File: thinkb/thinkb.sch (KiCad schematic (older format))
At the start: 128 parts, among them SW1 SW_Push, SW2 SW_Push, SW3 SW_Push, SW4 SW_Push, SW5 SW_Push, SW6 SW_Push

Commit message: Working on the PCB
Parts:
- removed D? (x6): 1N4148, Diode_THT:D_DO-35_SOD27_P7.62mm_Horizontal, symbol Diode:1N4148
- removed SW? (x6): SW_Push, footprints:Choc_PG1350_Choc_Spacing, symbol Switch:SW_Push
- added D50, D59: 1N4148, footprints:diode_TH_SMD, symbol Diode:1N4148
- added SW50, SW59: SW_Push, footprints:Choc_PG1350_Choc_Spacing, symbol Switch:SW_Push
- D1, D2, D3, D4, D5, D6: footprint Diode_THT:D_DO-35_SOD27_P7.62mm_Horizontal -> footprints:diode_TH_SMD
- D10, D11, D12, D13, D14, D15, D16, D17, D18, D19, D20, D21, D22, D23, D24, D25, D26, D27, D28, D29, D30, D31, D32, D33, D34, D35, D36, D37, D38, D39, D40, D41, D42, D43, D44, D45, D46, D47, D48, D49, D51, D52, D53, D54, D55, D56, D57, D58, D60, D7, D8, D9: renamed from D?; footprint Diode_THT:D_DO-35_SOD27_P7.62mm_Horizontal -> footprints:diode_TH_SMD
- gave numbers to parts that had none: 52
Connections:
- net col12 is gone; now on net col10: SW11.2, SW23.2, SW35.2, SW47.2
- net col13 is gone; now on net col11: SW12.2, SW24.2, SW36.2, SW48.2, SW60.2
- net col1: now also SW50.2
- net col10: now also SW59.2; no longer SW21.2, SW33.2, SW45.2, SW57.2, SW9.2
- net col11: no longer SW10.2, SW22.2, SW34.2, SW46.2, SW58.2
- net col6: now also SW19.2, SW31.2, SW43.2, SW55.2, SW7.2
- net col7: now also SW20.2, SW32.2, SW44.2, SW56.2, SW8.2
- net col8: now also SW21.2, SW33.2, SW45.2, SW57.2, SW9.2; no longer SW19.2, SW31.2, SW43.2, SW55.2, SW7.2
- net col9: now also SW10.2, SW22.2, SW34.2, SW46.2, SW58.2; no longer SW20.2, SW32.2, SW44.2, SW56.2, SW8.2
- net row4: now also D50.1 (K), D59.1 (K)
- new net: D50.2 (A), SW50.1
- new net: D59.2 (A), SW59.1
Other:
- moved on the sheet: D10, D11, D12, D19, D20, D21, D22, D23, D24, D31, D32, D33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

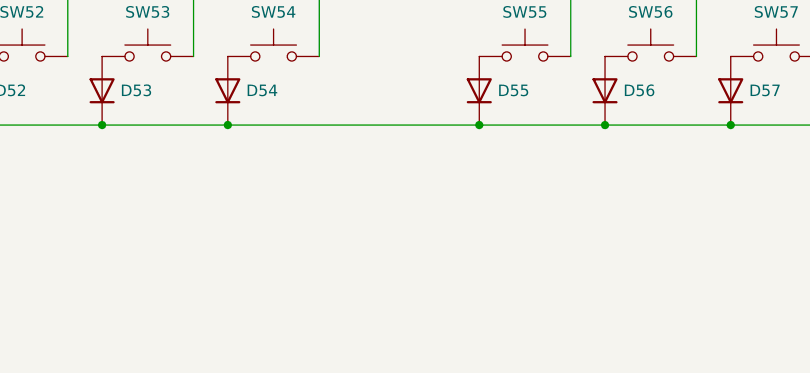
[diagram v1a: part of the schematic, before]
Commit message: Added rotary encoder
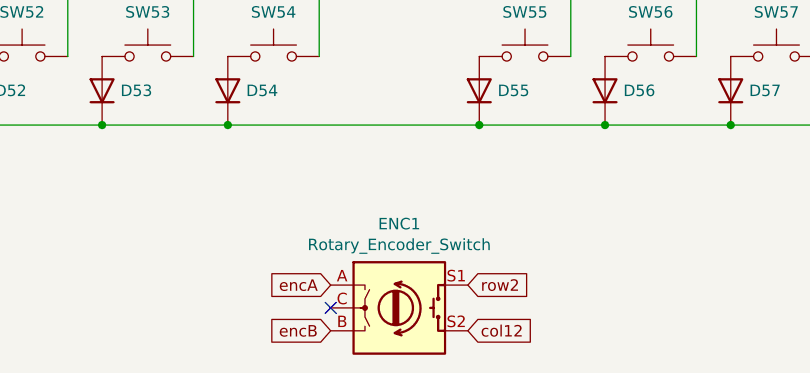
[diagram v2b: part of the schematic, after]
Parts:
- added ENC1: Rotary_Encoder_Switch, footprints:RotaryEncoder_Alps_EC11E, symbol Device:Rotary_Encoder_Switch
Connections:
- net row2: now also ENC1.S1
- new net col12: ENC1.S2
- new net encA: ENC1.A
- new net encB: ENC1.B
- no-connect marks 0 -> 1
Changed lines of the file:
@@
 	0    -1   -1   0
 $EndComp
+$Comp
+L Device:Rotary_Encoder_Switch ENC1
+U 1 1 616135F5
+P 4850 4700
+F 0 "ENC1" H 4850 5067 50  0000 C CNN
+F 1 "Rotary_Encoder_Switch" H 4850 4976 50  0000 C CNN
+F 2 "footprints:RotaryEncoder_Alps_EC11E" H 4700 4860 50  0001 C CNN
+F 3 "~" H 4850 4960 50  0001 C CNN
+	1    4850 4700
+	1    0    0    -1
+$EndComp
+Text GLabel 5150 4600 2    50   Input ~ 0
+row2
+Text GLabel 5150 4800 2    50   Input ~ 0
+col12
+Text GLabel 4550 4600 0    50   Input ~ 0
+encA
+NoConn ~ 4550 4700
+Text GLabel 4550 4800 0    50   Input ~ 0
+encB
 $EndSCHEMATC

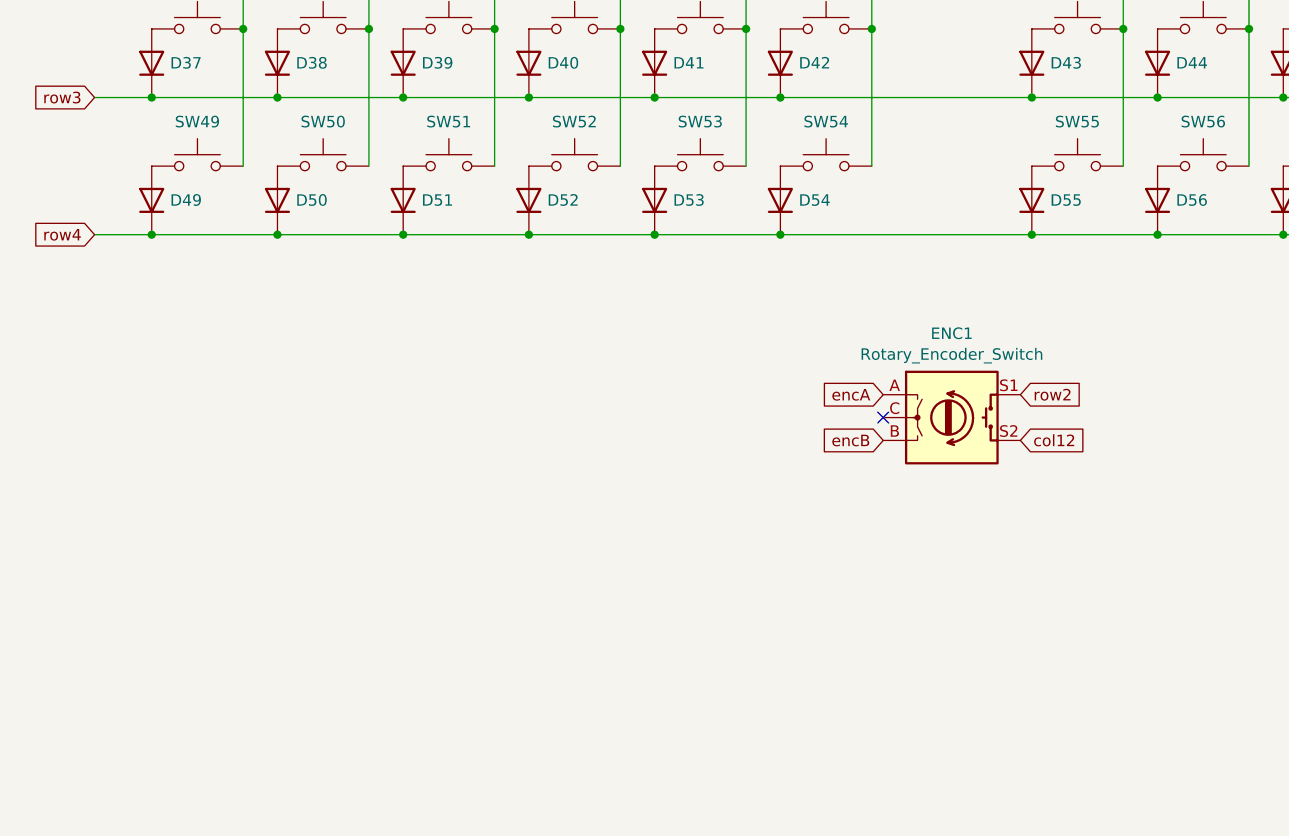
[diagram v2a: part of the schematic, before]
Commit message: Added promicro
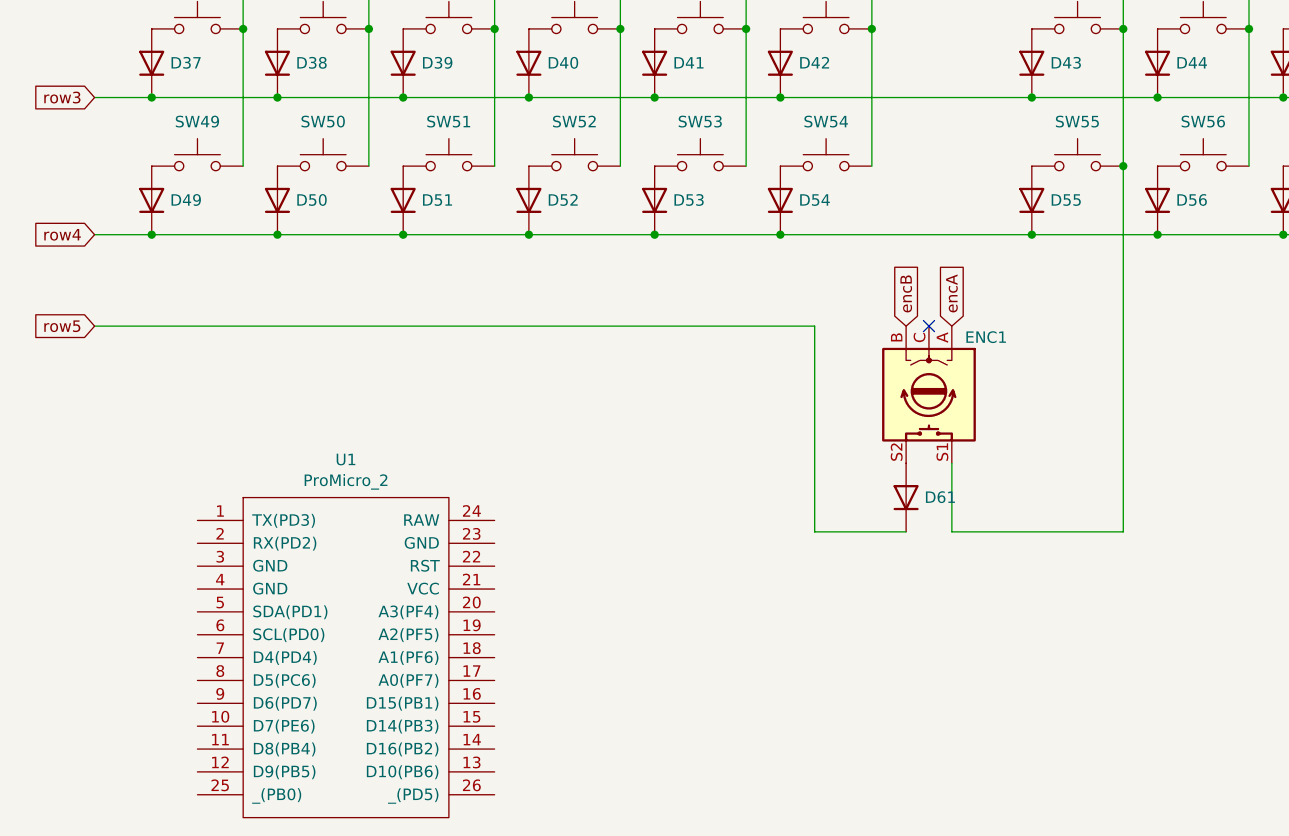
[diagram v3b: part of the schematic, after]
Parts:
- added D61: 1N4148, footprints:diode_TH_SMD, symbol Diode:1N4148
- added U1: ProMicro_2, footprints:ProMicro, symbol promicro_2:ProMicro_2
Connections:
- net col6: now also ENC1.S1
- net row2: no longer ENC1.S1
- net col12: no longer names the net of ENC1.S2
- net col12: now also D61.2 (A)
- new net row5: D61.1 (K)
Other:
- moved on the sheet: ENC1
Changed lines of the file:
@@
 	4100 2100 5200 2100
-Wire Wire Line
-	4100 2700 5200 2700
 Wire Wire Line
 	4100 3300 5200 3300
@@
 	0    -1   -1   0
 $EndComp
+Text GLabel 4850 4300 1    50   Input ~ 0
+encA
+NoConn ~ 4750 4300
+Text GLabel 4650 4300 1    50   Input ~ 0
+encB
+$Comp
+L Diode:1N4148 D61
+U 1 1 616F71C2
+P 4650 5050
+F 0 "D61" V 4650 4970 50  0000 R CNN
+F 1 "1N4148" H 4650 5176 50  0001 C CNN
+F 2 "footprints:diode_TH_SMD" H 4650 4875 50  0001 C CNN
+F 3 "https://assets.nexperia.com/documents/data-sheet/1N4148_1N4448.pdf" H 4650 5050 50  0001 C CNN
+	1    4650 5050
+	0    -1   -1   0
+$EndComp
 $Comp
 L Device:Rotary_Encoder_Switch ENC1
 U 1 1 616135F5
-P 4850 4700
-F 0 "ENC1" H 4850 5067 50  0000 C CNN
-F 1 "Rotary_Encoder_Switch" H 4850 4976 50  0000 C CNN
-F 2 "footprints:RotaryEncoder_Alps_EC11E" H 4700 4860 50  0001 C CNN
-F 3 "~" H 4850 4960 50  0001 C CNN
-	1    4850 4700
+P 4750 4600
+F 0 "ENC1" V 4500 4850 50  0000 C CNN
+F 1 "Rotary_Encoder_Switch" V 4500 5200 50  0001 C CNN
+F 2 "footprints:RotaryEncoder_Alps_EC11E" H 4600 4760 50  0001 C CNN
+F 3 "~" H 4750 4860 50  0001 C CNN
+	1    4750 4600
+	0    1    1    0
+$EndComp
+Wire Wire Line
+	4650 5200 4250 5200
+Wire Wire Line
+	4850 5200 4850 4900
+Wire Wire Line
+	4100 2700 5200 2700
+Text GLabel 1100 4300 0    50   Input ~ 0
+row5
+Wire Wire Line
+	1100 4300 4250 4300
+Wire Wire Line
+	4250 4300 4250 5200
+Wire Wire Line
+	5600 3600 5600 5200
+Wire Wire Line
+	5600 5200 4850 5200
+Connection ~ 5600 3600
+$Comp
+L promicro_2:ProMicro_2 U1
+U 1 1 6198CAAD
+P 2200 5700
+F 0 "U1" H 2200 6515 50  0000 C CNN
+F 1 "ProMicro_2" H 2200 6424 50  0000 C CNN
+F 2 "footprints:ProMicro" H 2150 5800 50  0001 C CNN
+F 3 "" H 2150 5800 50  0001 C CNN
+	1    2200 5700
 	1    0    0    -1
 $EndComp
-Text GLabel 5150 4600 2    50   Input ~ 0
-row2
-Text GLabel 5150 4800 2    50   Input ~ 0
-col12
-Text GLabel 4550 4600 0    50   Input ~ 0
-encA
-NoConn ~ 4550 4700
-Text GLabel 4550 4800 0    50   Input ~ 0
-encB
 $EndSCHEMATC

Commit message: Trying to implement more sophisticated row/col scheme
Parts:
- removed D10, D11, D12, D21, D22, D23, D24, D33, D34, D35, D36, D45, D46, D47, D48, D57, D58, D59, D60, D61, D9: 1N4148, footprints:diode_TH_SMD, symbol Diode:1N4148
- removed SW10, SW11, SW12, SW21, SW22, SW23, SW24, SW33, SW34, SW35, SW36, SW45, SW46, SW47, SW48, SW57, SW58, SW59, SW60, SW9: SW_Push, footprints:Choc_PG1350_Choc_Spacing, symbol Switch:SW_Push
- added D? (x23): 1N4148, footprints:diode_TH_SMD, symbol Diode:1N4148
- added SW? (x23): SW_Push, footprints:Choc_PG1350_Choc_Spacing, symbol Switch:SW_Push
- renumbered D13 to D9, SW13 to SW9
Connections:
- net col0: now also SW?.2, SW?.2, SW?.2
- net col1: now also SW?.2, SW?.2, SW?.2
- net col2: now also SW?.2, SW?.2, SW?.2
- net col3: now also ENC1.S2, SW?.2, SW?.2, SW?.2
- net col4: now also SW?.2, SW?.2
- net col5: now also SW?.2, SW?.2, SW?.2
- net col6: now also SW?.2, SW?.2, SW?.2; no longer ENC1.S1
- net col7: now also SW?.2, SW?.2, SW?.2
- net row5: now also D?.1 (K), D?.1 (K), D?.1 (K), D?.1 (K), D?.1 (K), D?.1 (K), D?.1 (K), D?.1 (K)
- new net: D?.2 (A), ENC1.S1, SW?.1
- new net: D?.2 (A), SW?.1 (x22)
- new net row6: D?.1 (K), D?.1 (K), D?.1 (K), D?.1 (K), D?.1 (K), D?.1 (K), D?.1 (K), D?.1 (K)
- new net row7: D?.1 (K), D?.1 (K), D?.1 (K), D?.1 (K), D?.1 (K), D?.1 (K), D?.1 (K)
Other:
- moved on the sheet: D17, D18, D29, D30, D41, D42, D5, D53, D54, D6, ENC1, SW17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

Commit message: WIP on keyboard matrix
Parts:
- removed D17, D4, D5: 1N4148, footprints:diode_TH_SMD, symbol Diode:1N4148
- removed SW17, SW4, SW5: SW_Push, footprints:Choc_PG1350_Choc_Spacing, symbol Switch:SW_Push
- added D58: 1N4148, footprints:diode_TH_SMD, symbol Diode:1N4148
- added SW58: SW_Push, footprints:Choc_PG1350_Choc_Spacing, symbol Switch:SW_Push
- gave numbers to parts that had none: 46
- renumbered D16 to D10, D18 to D11, D19 to D12, D20 to D13, D25 to D14, D26 to D15, D27 to D16, D28 to D17, D29 to D18, D30 to D19, D31 to D20, D32 to D21, D37 to D22, D38 to D23, D39 to D24, D40 to D25, D41 to D26, D42 to D27, D43 to D28, D44 to D29, D49 to D30, D50 to D31, D51 to D32, D52 to D33, D53 to D34, D54 to D35, D55 to D36, D56 to D37, D6 to D4, D7 to D5, D8 to D6, D9 to D7, D14 to D8, D15 to D9, SW16 to SW10, SW18 to SW11, SW19 to SW12, SW20 to SW13, SW25 to SW14, SW26 to SW15, SW27 to SW16, SW28 to SW17, SW29 to SW18, SW30 to SW19, SW31 to SW20, SW32 to SW21, SW37 to SW22, SW38 to SW23, SW39 to SW24, SW40 to SW25, SW41 to SW26, SW42 to SW27, SW43 to SW28, SW44 to SW29, SW49 to SW30, SW50 to SW31, SW51 to SW32, SW52 to SW33, SW53 to SW34, SW54 to SW35, SW55 to SW36, SW56 to SW37, SW6 to SW4, SW7 to SW5, SW8 to SW6, SW9 to SW7, SW14 to SW8, SW15 to SW9
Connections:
- net col3: now also ENC1.S1; no longer ENC1.S2
- net col4: now also SW58.2
- net row7: now also D58.1 (K)
- net at D10.2 (A), SW10.1: now also ENC1.S2
- net at D57.2 (A), SW57.1: no longer ENC1.S1
- new net: D58.2 (A), SW58.1
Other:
- moved on the sheet: D1, D10, D11, D12, D13, D14, D15, D16, D17, D18, D19, D2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

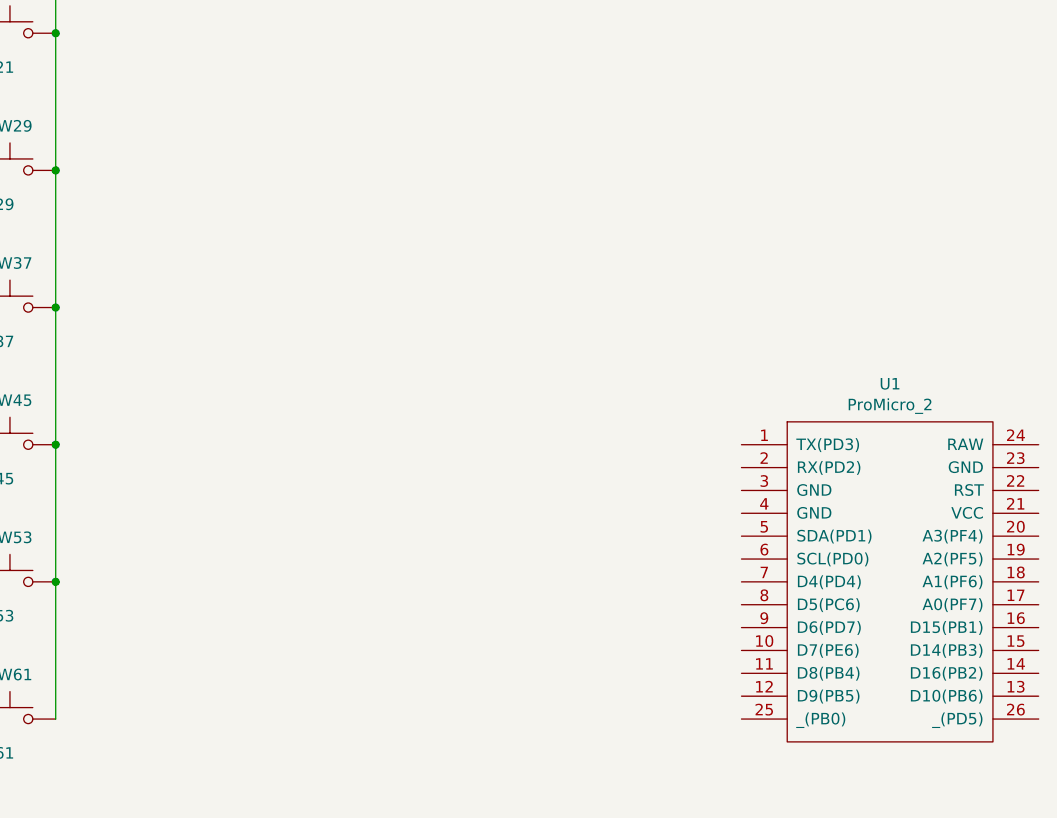
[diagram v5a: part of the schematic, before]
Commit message: Added more symbols to the schema
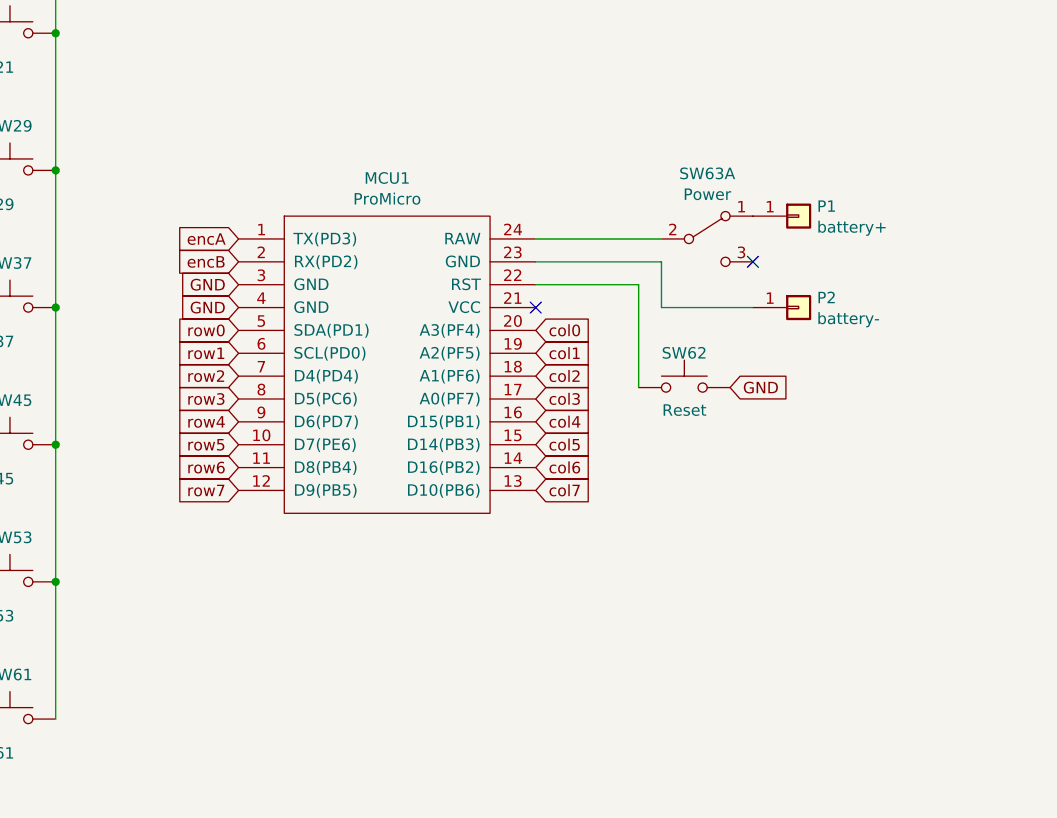
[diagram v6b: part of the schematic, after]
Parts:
- removed U1: ProMicro_2, footprints:ProMicro, symbol promicro_2:ProMicro_2
- added MCU1: ProMicro, footprints:ProMicro, symbol promicro:ProMicro_2
- added P1: battery+, footprints:1pin_conn, symbol pin_pad:i2c_pin
- added P2: battery-, footprints:1pin_conn, symbol pin_pad:i2c_pin
- added SW62: Reset, footprints:Switch_Reset_THT, symbol Switch:SW_Push
- added SW63: Power, footprints:Switch_MSK-12C01-07, symbol Switch:SW_DPDT_x2
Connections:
- net col0: now also MCU1.20 (A3(PF4))
- net col1: now also MCU1.19 (A2(PF5))
- net col2: now also MCU1.18 (A1(PF6))
- net col3: now also MCU1.17 (A0(PF7))
- net col4: now also MCU1.16 (D15(PB1))
- net col5: now also MCU1.15 (D14(PB3))
- net col6: now also MCU1.14 (D16(PB2))
- net col7: now also MCU1.13 (D10(PB6))
- net encA: now also MCU1.1 (TX(PD3))
- net encB: now also MCU1.2 (RX(PD2))
- net row0: now also MCU1.5 (SDA(PD1))
- net row1: now also MCU1.6 (SCL(PD0))
- net row2: now also MCU1.7 (D4(PD4))
- net row3: now also MCU1.8 (D5(PC6))
- net row4: now also MCU1.9 (D6(PD7))
- net row5: now also MCU1.10 (D7(PE6))
- net row6: now also MCU1.11 (D8(PB4))
- net row7: now also MCU1.12 (D9(PB5))
- new net: P1.1 (Pin_1), SW63.1 (A)
- new net: MCU1.23 (GND), P2.1 (Pin_1)
- new net: MCU1.22 (RST), SW62.1
- new net: MCU1.24 (RAW), SW63.2 (B)
- new net GND: MCU1.3 (GND), MCU1.4 (GND), SW62.2
- no-connect marks 1 -> 3
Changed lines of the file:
@@
-$EndComp
-$Comp
-L promicro_2:ProMicro_2 U1
-U 1 1 6198CAAD
-P 10150 5150
-F 0 "U1" H 10150 5965 50  0000 C CNN
-F 1 "ProMicro_2" H 10150 5874 50  0000 C CNN
-F 2 "footprints:ProMicro" H 10100 5250 50  0001 C CNN
-F 3 "" H 10100 5250 50  0001 C CNN
-	1    10150 5150
-	1    0    0    -1
 $EndComp
 $Comp
@@
 	4450 6100 5000 6100
 Connection ~ 4850 5200
+$Comp
+L promicro:ProMicro_2 MCU1
+U 1 1 6156E83C
+P 7950 4250
+F 0 "MCU1" H 7950 5065 50  0000 C CNN
+F 1 "ProMicro" H 7950 4974 50  0000 C CNN
+F 2 "footprints:ProMicro" H 7900 4350 50  0001 C CNN
+F 3 "" H 7900 4350 50  0001 C CNN
+	1    7950 4250
+	1    0    0    -1
+$EndComp
+Text GLabel 7300 4100 0    50   Input ~ 0
+row0
+Text GLabel 7300 4200 0    50   Input ~ 0
+row1
+Text GLabel 7300 4300 0    50   Input ~ 0
+row2
+Text GLabel 7300 4400 0    50   Input ~ 0
+row3
+Text GLabel 7300 4500 0    50   Input ~ 0
+row4
+Text GLabel 7300 4600 0    50   Input ~ 0
+row5
+Text GLabel 7300 4700 0    50   Input ~ 0
+row6
+Text GLabel 7300 4800 0    50   Input ~ 0
+row7
+Text GLabel 8600 4100 2    50   Input ~ 0
+col0
+Text GLabel 8600 4200 2    50   Input ~ 0
+col1
+Text GLabel 8600 4300 2    50   Input ~ 0
+col2
+Text GLabel 8600 4400 2    50   Input ~ 0
+col3
+Text GLabel 8600 4500 2    50   Input ~ 0
+col4
+Text GLabel 8600 4600 2    50   Input ~ 0
+col5
+Text GLabel 8600 4700 2    50   Input ~ 0
+col6
+Text GLabel 8600 4800 2    50   Input ~ 0
+col7
+Text GLabel 7300 3700 0    50   Input ~ 0
+encA
+Text GLabel 7300 3800 0    50   Input ~ 0
+encB
+$Comp
+L Switch:SW_Push SW62
+U 1 1 615EC03C
+P 9250 4350
+F 0 "SW62" H 9250 4500 50  0000 C CNN
+F 1 "Reset" H 9250 4250 50  0000 C CNN
+F 2 "footprints:Switch_Reset_THT" H 9250 4550 50  0001 C CNN
+F 3 "~" H 9250 4550 50  0001 C CNN
+	1    9250 4350
+	1    0    0    -1
+$EndComp
+Wire Wire Line
+	8600 3900 9050 3900
+Text GLabel 9450 4350 2    50   Input ~ 0
+GND
+Text GLabel 7300 3900 0    50   Input ~ 0
+GND
+Text GLabel 7300 4000 0    50   Input ~ 0
+GND
+NoConn ~ 8600 4000
+$Comp
+L Switch:SW_DPDT_x2 SW63
+U 1 1 6164490B
+P 9350 3700
+F 0 "SW63" H 9350 3985 50  0000 C CNN
+F 1 "Power" H 9350 3894 50  0000 C CNN
+F 2 "footprints:Switch_MSK-12C01-07" H 9350 3700 50  0001 C CNN
+F 3 "~" H 9350 3700 50  0001 C CNN
+	1    9350 3700
+	1    0    0    -1
+$EndComp
+$Comp
+L pin_pad:i2c_pin P1
+U 1 1 6151B959
+P 9750 3600
+F 0 "P1" H 9830 3642 50  0000 L CNN
+F 1 "battery+" H 9830 3551 50  0000 L CNN
+F 2 "footprints:1pin_conn" H 9750 3600 50  0001 C CNN
+F 3 "" H 9750 3600 50  0001 C CNN
+	1    9750 3600
+	1    0    0    -1
+$EndComp
+$Comp
+L pin_pad:i2c_pin P2
+U 1 1 6151CDBA
+P 9750 4000
+F 0 "P2" H 9830 4042 50  0000 L CNN
+F 1 "battery-" H 9830 3951 50  0000 L CNN
+F 2 "footprints:1pin_conn" H 9750 4000 50  0001 C CNN
+F 3 "" H 9750 4000 50  0001 C CNN
+	1    9750 4000
+	1    0    0    -1
+$EndComp
+Wire Wire Line
+	9050 3900 9050 4350
+Wire Wire Line
+	9150 3700 8600 3700
+NoConn ~ 9550 3800
+Wire Wire Line
+	9550 4000 9150 4000
+Wire Wire Line
+	9150 4000 9150 3800
+Wire Wire Line
+	9150 3800 8600 3800
 $EndSCHEMATC

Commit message: Renumbered switches on the pcb
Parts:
- removed SW10: SW_Push, footprints:Choc_PG1350_Choc_Spacing, symbol Switch:SW_Push
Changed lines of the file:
@@
 Connection ~ 2250 2500
-$Comp
-L Switch:SW_Push SW10
-U 1 1 61529B5C
-P 3550 2200
-F 0 "SW10" H 3550 2393 50  0000 C CNN
-F 1 "SW_Push" H 3550 2394 50  0001 C CNN
-F 2 "footprints:Choc_PG1350_Choc_Spacing" H 3550 2400 50  0001 C CNN
-F 3 "~" H 3550 2400 50  0001 C CNN
-	1    3550 2200
-	1    0    0    -1
-$EndComp
 $Comp
 L Diode:1N4148 D10
@@
 Wire Wire Line
 	3350 1800 3350 2200
-Connection ~ 3350 2200
 Wire Wire Line
 	4850 1300 4850 2800

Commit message: Changed switch footprint
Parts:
- SW1, SW11, SW12, SW13, SW14, SW15, SW16, SW17, SW18, SW19, SW2, SW20, SW21, SW22, SW23, SW24, SW25, SW26, SW27, SW28, SW29, SW3, SW30, SW31, SW32, SW33, SW34, SW35, SW36, SW37, SW38, SW39, SW4, SW40, SW41, SW42, SW43, SW44, SW45, SW46, SW47, SW48, SW49, SW5, SW50, SW51, SW52, SW53, SW54, SW55, SW56, SW57, SW58, SW59, SW6, SW60, SW61, SW7, SW8, SW9: footprint footprints:Choc_PG1350_Choc_Spacing -> footprints:Kailh_socket_PG1350_optional
